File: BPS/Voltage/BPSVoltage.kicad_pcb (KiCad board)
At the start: 2 copper layers, 75 x 65 mm, 124 parts, among them J1 Conn1, J2 Conn2, J3 Conn_01x06, J4 Conn_01x07, J5 Conn_01x03, J6 Conn_01x05, J7 Conn_01x05, Q1 BSS308PE, Q10 BSS308PE, Q11 BSS308PE, Q12 BSS308PE, Q13 BSS308PE, Q2 BSS308PE, Q3 BSS308PE, Q4 BSS308PE, Q5 NSV1C201MZ4, Q6 BSS308PE, Q7 BSS308PE, Q8 BSS308PE, Q9 BSS308PE, U1 LTC6811-1, U2 HX1188FNL

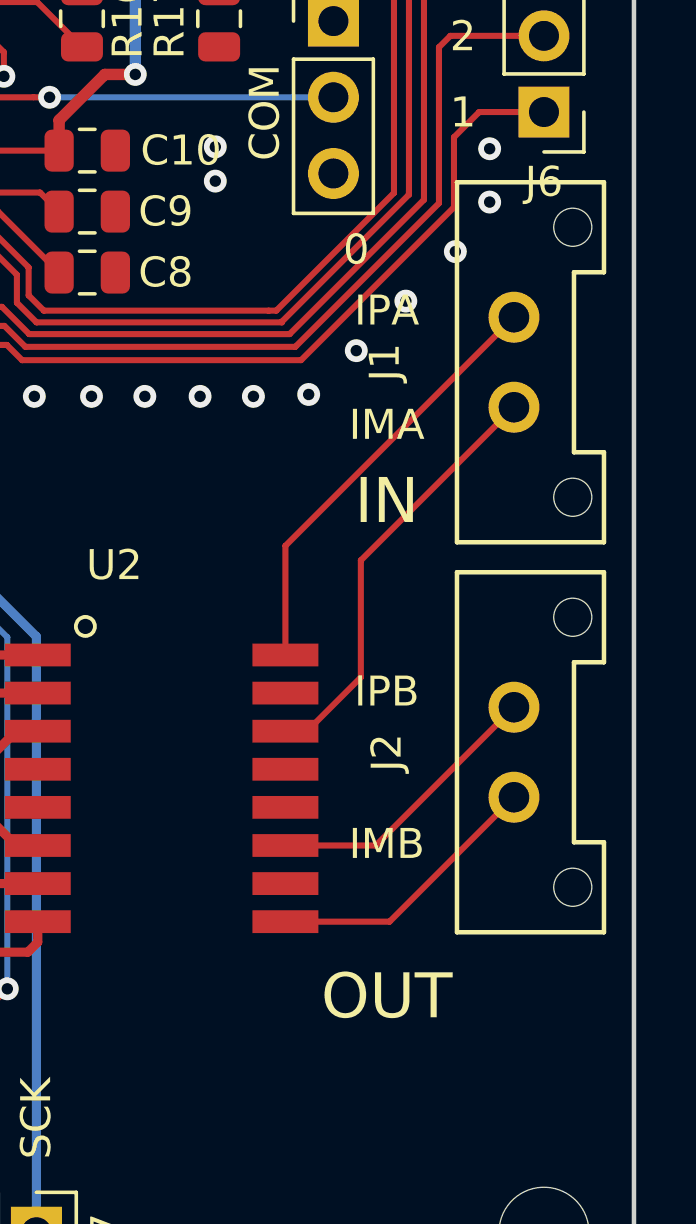
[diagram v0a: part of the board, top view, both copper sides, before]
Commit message: Changed the connectors to stack
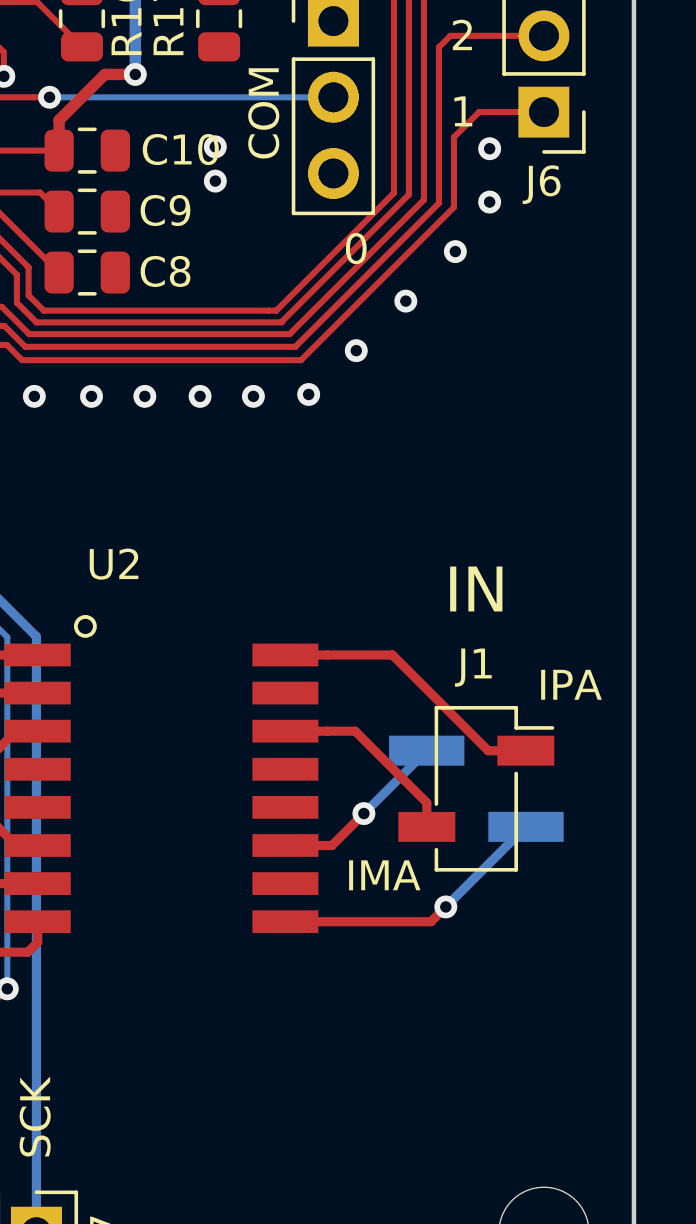
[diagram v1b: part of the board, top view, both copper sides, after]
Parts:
- J1: footprint UTSVT_Connectors:Molex_MicroFit3.0_1x2xP3.00mm_PolarizingPeg_Vertical -> Connector_PinSocket_2.54mm:PinSocket_1x02_P2.54mm_Vertical_SMD_Pin1Right
- J2: footprint UTSVT_Connectors:Molex_MicroFit3.0_1x2xP3.00mm_PolarizingPeg_Vertical -> Connector_PinHeader_2.54mm:PinHeader_1x02_P2.54mm_Vertical_SMD_Pin1Right; moved to B.Cu
- moved J1 15.8 mm to (114.7, 97.2), turned to 0 degrees
- moved J2 2.99 mm to (114.7, 97.2), turned to 180 degrees
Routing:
- net Net-(J1-Pad2): track 14.4 -> 6.51 mm
- net Net-(J1-Pad1): track 14.4 -> 9.33 mm
- net Net-(J2-Pad1): track 9.53 -> 6.02 mm, vias 0 -> 1
- net Net-(J2-Pad2): track 9.34 -> 9.33 mm, vias 0 -> 1

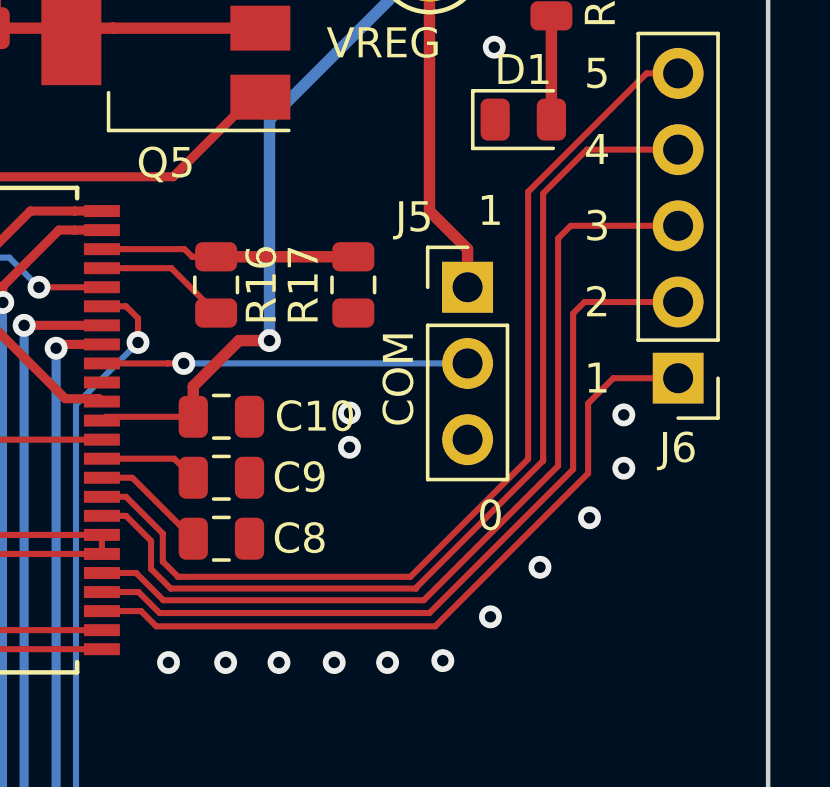
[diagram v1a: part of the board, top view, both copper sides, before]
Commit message: Edited comm pins of BPS voltage in case of stacking issues.
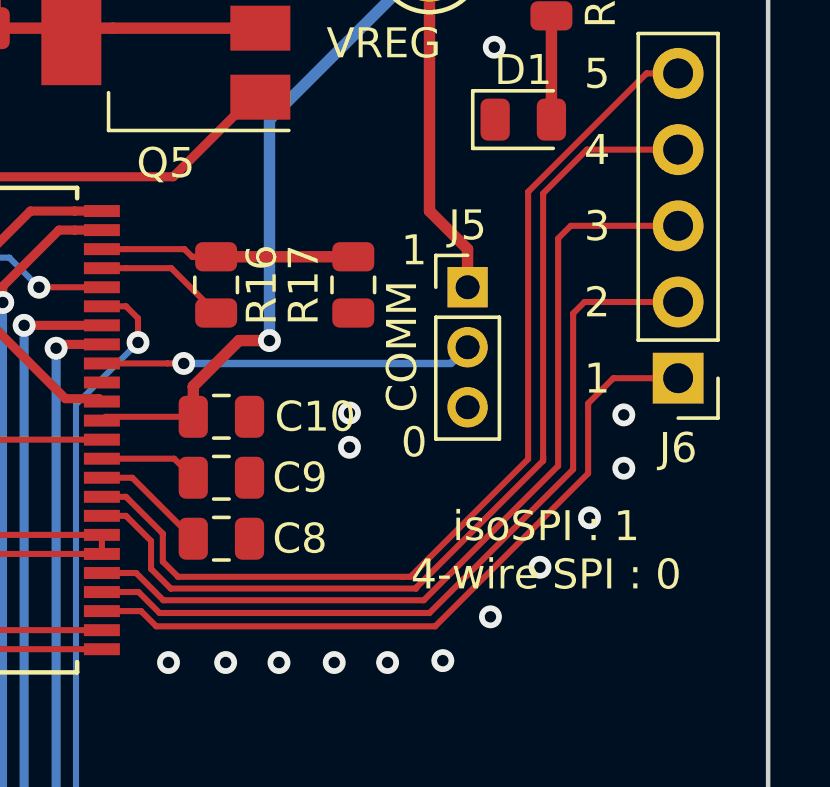
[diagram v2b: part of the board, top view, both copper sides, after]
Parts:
- J5: footprint Connector_PinHeader_2.54mm:PinHeader_1x03_P2.54mm_Vertical -> Connector_PinHeader_2.00mm:PinHeader_1x03_P2.00mm_Vertical
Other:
- board text added: "COMM"
- board text added: "isoSPI : 1 4-wire SPI : 0"
- board text removed: "COM"
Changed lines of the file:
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@@
   (general
     (thickness 1.6)
-    (drawings 38)
-    (tracks 661)
+    (drawings 39)
+    (tracks 662)
     (zones 0)
     (modules 124)
@@
   )
   (setup
-    (last_trace_width 0.3048)
+    (last_trace_width 0.25)
     (user_trace_width 0.2032)
     (user_trace_width 0.254)
@@
     (add_net "Net-(R16-Pad2)")
   )
+  (module Connector_PinHeader_2.00mm:PinHeader_1x03_P2.00mm_Vertical (layer F.Cu)
+    (at 109.982 71.628)
+    (descr "Through hole straight pin header, 1x03, 2.00mm pitch, single row")
+    (tags "Through hole pin header THT 1x03 2.00mm single row")
+    (fp_text reference J5 (at 0 -2.06) (layer F.SilkS)
+      (effects (font (size 1 1) (thickness 0.15)))
+    )
+    (fp_text value Conn_01x03 (at 0 6.06) (layer F.Fab)
+      (effects (font (size 1 1) (thickness 0.15)))
+    )
+    (fp_text user %R (at 0 2 90) (layer F.Fab)
+      (effects (font (size 1 1) (thickness 0.15)))
+    )
+    (fp_line (start 1.5 -1.5) (end -1.5 -1.5) (layer F.CrtYd) (width 0.05))
+    (fp_line (start 1.5 5.5) (end 1.5 -1.5) (layer F.CrtYd) (width 0.05))
+    (fp_line (start -1.5 5.5) (end 1.5 5.5) (layer F.CrtYd) (width 0.05))
+    (fp_line (start -1.5 -1.5) (end -1.5 5.5) (layer F.CrtYd) (width 0.05))
+    (fp_line (start -1.06 -1.06) (end 0 -1.06) (layer F.SilkS) (width 0.12))
+    (fp_line (start -1.06 0) (end -1.06 -1.06) (layer F.SilkS) (width 0.12))
+    (fp_line (start -1.06 1) (end 1.06 1) (layer F.SilkS) (width 0.12))
+    (fp_line (start 1.06 1) (end 1.06 5.06) (layer F.SilkS) (width 0.12))
+    (fp_line (start -1.06 1) (end -1.06 5.06) (layer F.SilkS) (width 0.12))
+    (fp_line (start -1.06 5.06) (end 1.06 5.06) (layer F.SilkS) (width 0.12))
+    (fp_line (start -1 -0.5) (end -0.5 -1) (layer F.Fab) (width 0.1))
+    (fp_line (start -1 5) (end -1 -0.5) (layer F.Fab) (width 0.1))
+    (fp_line (start 1 5) (end -1 5) (layer F.Fab) (width 0.1))
+    (fp_line (start 1 -1) (end 1 5) (layer F.Fab) (width 0.1))
+    (fp_line (start -0.5 -1) (end 1 -1) (layer F.Fab) (width 0.1))
+    (pad 3 thru_hole oval (at 0 4) (size 1.35 1.35) (drill 0.8) (layers *.Cu *.Mask)
+      (net 2 GND))
+    (pad 2 thru_hole oval (at 0 2) (size 1.35 1.35) (drill 0.8) (layers *.Cu *.Mask)
+      (net 59 /ISOMD))
+    (pad 1 thru_hole rect (at 0 0) (size 1.35 1.35) (drill 0.8) (layers *.Cu *.Mask)
+      (net 12 /VREG))
+    (model ${KISYS3DMOD}/Connector_PinHeader_2.00mm.3dshapes/PinHeader_1x03_P2.00mm_Vertical.wrl
+      (at (xyz 0 0 0))
+      (scale (xyz 1 1 1))
+      (rotate (xyz 0 0 0))
+    )
+  )
   (module MountingHole:MountingHole_3mm (layer F.Cu)
     (at 48 53)
@@
     )
   )
-  (module Connector_PinHeader_2.54mm:PinHeader_1x03_P2.54mm_Vertical (layer F.Cu)
-    (at 109.982 71.628)
-    (descr "Through hole straight pin header, 1x03, 2.54mm pitch, single row")
-    (tags "Through hole pin header THT 1x03 2.54mm single row")
-    (fp_text reference J5 (at -1.778 -2.33) (layer F.SilkS)
-      (effects (font (size 1 1) (thickness 0.15)))
-    )
-    (fp_text value Conn_01x03 (at 0 7.41) (layer F.Fab)
-      (effects (font (size 1 1) (thickness 0.15)))
-    )
-    (fp_line (start -0.635 -1.27) (end 1.27 -1.27) (layer F.Fab) (width 0.1))
-    (fp_line (start 1.27 -1.27) (end 1.27 6.35) (layer F.Fab) (width 0.1))
-    (fp_line (start 1.27 6.35) (end -1.27 6.35) (layer F.Fab) (width 0.1))
-    (fp_line (start -1.27 6.35) (end -1.27 -0.635) (layer F.Fab) (width 0.1))
-    (fp_line (start -1.27 -0.635) (end -0.635 -1.27) (layer F.Fab) (width 0.1))
-    (fp_line (start -1.33 6.41) (end 1.33 6.41) (layer F.SilkS) (width 0.12))
-    (fp_line (start -1.33 1.27) (end -1.33 6.41) (layer F.SilkS) (width 0.12))
-    (fp_line (start 1.33 1.27) (end 1.33 6.41) (layer F.SilkS) (width 0.12))
-    (fp_line (start -1.33 1.27) (end 1.33 1.27) (layer F.SilkS) (width 0.12))
-    (fp_line (start -1.33 0) (end -1.33 -1.33) (layer F.SilkS) (width 0.12))
-    (fp_line (start -1.33 -1.33) (end 0 -1.33) (layer F.SilkS) (width 0.12))
-    (fp_line (start -1.8 -1.8) (end -1.8 6.85) (layer F.CrtYd) (width 0.05))
-    (fp_line (start -1.8 6.85) (end 1.8 6.85) (layer F.CrtYd) (width 0.05))
-    (fp_line (start 1.8 6.85) (end 1.8 -1.8) (layer F.CrtYd) (width 0.05))
-    (fp_line (start 1.8 -1.8) (end -1.8 -1.8) (layer F.CrtYd) (width 0.05))
-    (fp_text user %R (at 0 2.54 90) (layer F.Fab)
-      (effects (font (size 1 1) (thickness 0.15)))
-    )
-    (pad 1 thru_hole rect (at 0 0) (size 1.7 1.7) (drill 1) (layers *.Cu *.Mask)
-      (net 12 /VREG))
-    (pad 2 thru_hole oval (at 0 2.54) (size 1.7 1.7) (drill 1) (layers *.Cu *.Mask)
-      (net 59 /ISOMD))
-    (pad 3 thru_hole oval (at 0 5.08) (size 1.7 1.7) (drill 1) (layers *.Cu *.Mask)
-      (net 2 GND))
-    (model ${KISYS3DMOD}/Connector_PinHeader_2.54mm.3dshapes/PinHeader_1x03_P2.54mm_Vertical.wrl
-      (at (xyz 0 0 0))
-      (scale (xyz 1 1 1))
-      (rotate (xyz 0 0 0))
-    )
-  )
   (module Connector_PinHeader_2.54mm:PinHeader_1x05_P2.54mm_Vertical (layer F.Cu)
     (at 117 74.66 180)
@@
     )
   )
+  (gr_text "isoSPI : 1\n4-wire SPI : 0" (at 112.6 80.4) (layer F.SilkS)
+    (effects (font (size 1 1) (thickness 0.15)))
+  )
   (gr_text "Dr. Gary Hallock" (at 99.1 102.35) (layer B.SilkS)
     (effects (font (size 1.5 1.5) (thickness 0.3)) (justify mirror))
@@
     (effects (font (size 1 1) (thickness 0.15)))
   )
-  (gr_text COM (at 107.696 74.676 90) (layer F.SilkS)
+  (gr_text COMM (at 107.8 73.6 90) (layer F.SilkS)
     (effects (font (size 1 1) (thickness 0.15)))
   )
-  (gr_text 1 (at 110.744 69.088) (layer F.SilkS)
+  (gr_text 1 (at 108.2 70.4) (layer F.SilkS)
     (effects (font (size 1 1) (thickness 0.15)))
   )
-  (gr_text 0 (at 110.744 79.248) (layer F.SilkS)
+  (gr_text 0 (at 108.2 76.8) (layer F.SilkS)
     (effects (font (size 1 1) (thickness 0.15)))
   )
@@
   (segment (start 103.378 73.406) (end 103.378 66.04) (width 0.381) (layer B.Cu) (net 12))
   (segment (start 108.712 60.706) (end 108.712 69.088) (width 0.381) (layer F.Cu) (net 12) (status 10))
-  (segment (start 109.982 70.358) (end 109.982 71.628) (width 0.381) (layer F.Cu) (net 12) (status 20))
   (segment (start 108.712 69.088) (end 109.982 70.358) (width 0.381) (layer F.Cu) (net 12))
+  (segment (start 109.982 70.358) (end 109.982 71.782) (width 0.381) (layer F.Cu) (net 12))
   (via (at 74.676 81.05546) (size 0.762) (drill 0.381) (layers F.Cu B.Cu) (net 13))
   (segment (start 74.58557 80.96503) (end 74.676 81.05546) (width 0.381) (layer F.Cu) (net 13))
@@
   (segment (start 112.776 62.581) (end 112.776 66.04) (width 0.381) (layer F.Cu) (net 58) (status 30))
   (via (at 100.5205 74.168) (size 0.762) (drill 0.381) (layers F.Cu B.Cu) (net 59))
-  (segment (start 109.982 74.168) (end 100.5205 74.168) (width 0.2032) (layer B.Cu) (net 59) (status 10))
   (segment (start 99.981685 74.168) (end 97.792 74.168) (width 0.2032) (layer F.Cu) (net 59) (status 20))
   (segment (start 100.5205 74.168) (end 99.981685 74.168) (width 0.2032) (layer F.Cu) (net 59))
+  (segment (start 100.5205 74.168) (end 109.432 74.168) (width 0.25) (layer B.Cu) (net 59))
+  (segment (start 109.432 74.168) (end 110 73.6) (width 0.25) (layer B.Cu) (net 59))
   (segment (start 99.822 79.8398) (end 98.5952 78.613) (width 0.2032) (layer F.Cu) (net 60))
   (segment (start 99.822 80.772) (end 99.822 79.8398) (width 0.2032) (layer F.Cu) (net 60))

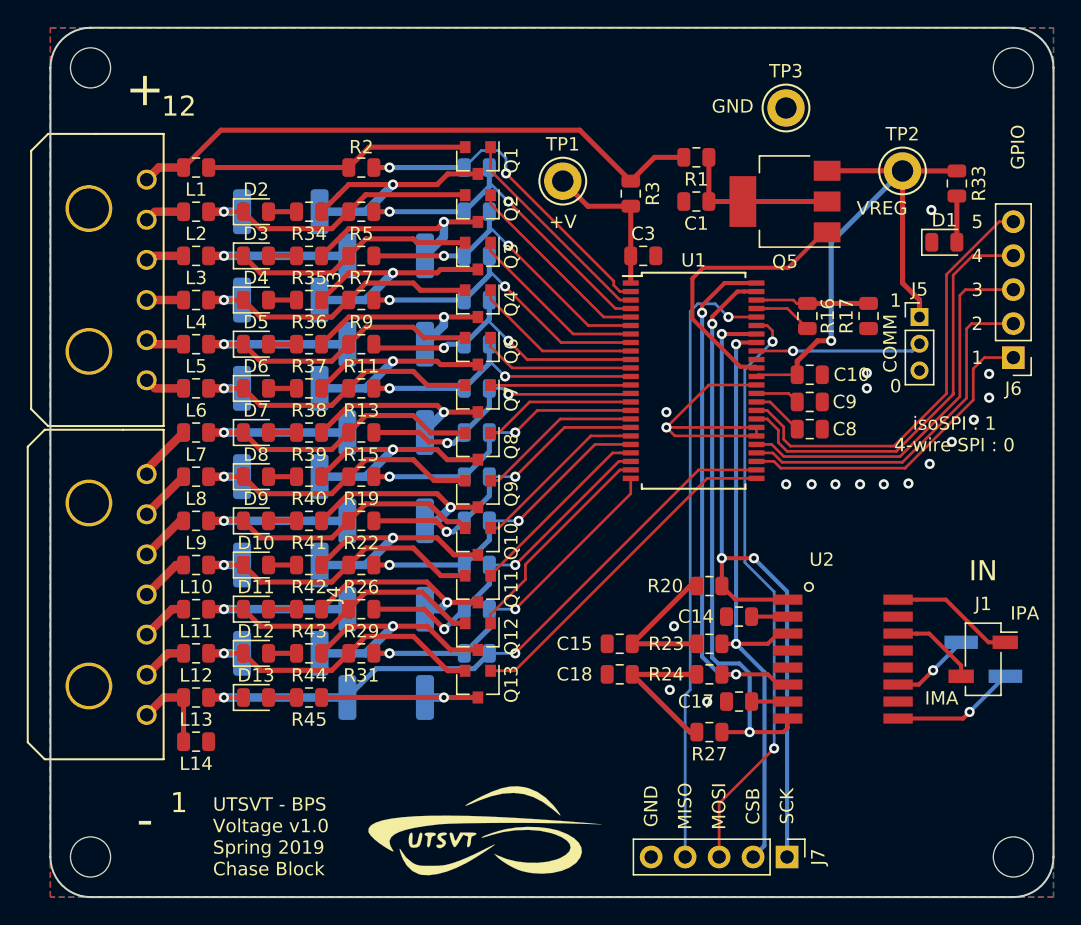
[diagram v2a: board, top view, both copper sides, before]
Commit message: Redid the footprint for the IC, rerouted.
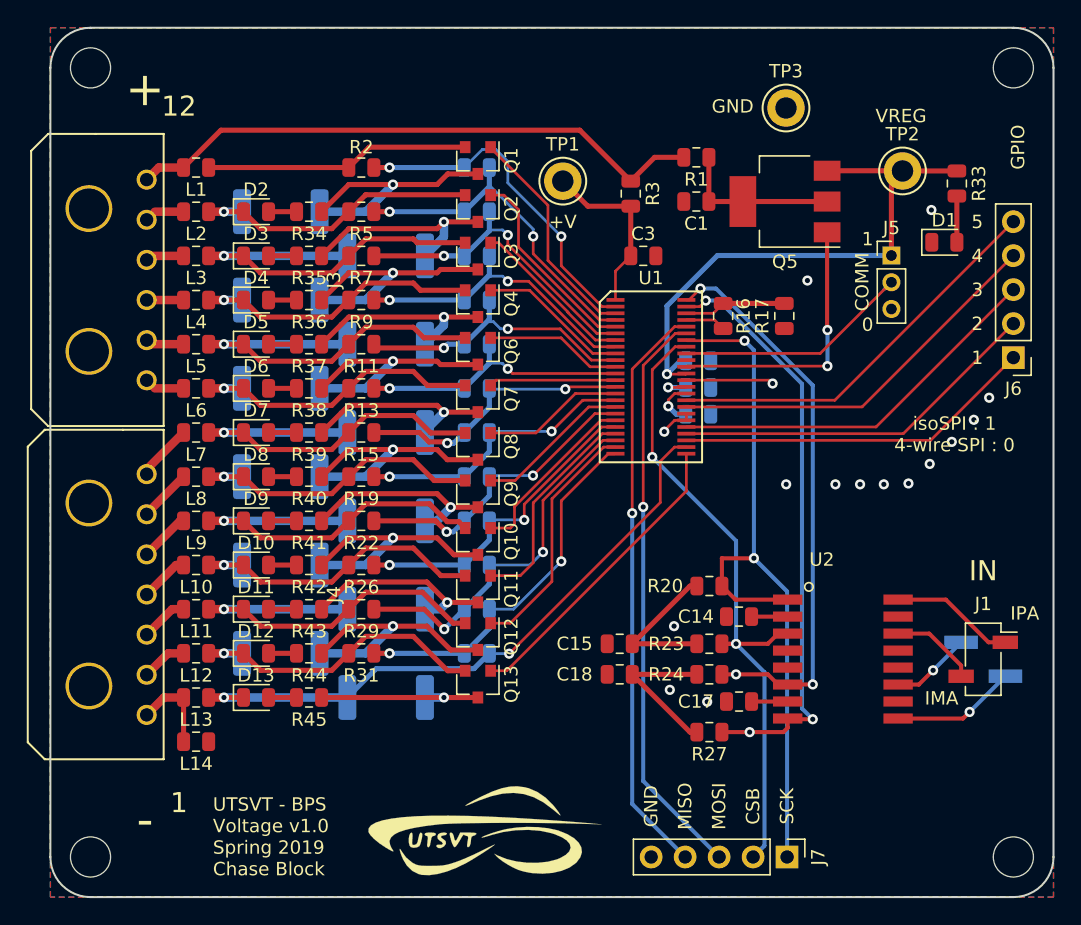
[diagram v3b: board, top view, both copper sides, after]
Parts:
- C10, C8, C9: moved to B.Cu
- U1: footprint Package_SO:SSOP-48_7.5x15.9mm_P0.635mm -> UTSVT_ICs:SOIC-48
- moved C8 8.41 mm to (93.4, 78.9)
- moved C9 8.41 mm to (93.4, 76.9)
- moved C10 8.40 mm to (93.4, 74.9)
- moved G*** 7.25 mm to (102.0, 91.5)
- moved R16 6.30 mm to (95.3, 71.5)
- moved R17 6.30 mm to (99.9, 71.5)
- moved J5 5.06 mm to (107.9, 67.0)
- moved U1 3.21 mm to (89.9, 76.1), turned to 270 degrees
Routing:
- net GND: track 22.4 -> 9.10 mm, vias 19 -> 16
- net /ISOMD: track 12.4 -> 18.3 mm, vias 1 -> 0
- net /SDO: track 46.5 -> 43.5 mm
- net /GPIO4: track 32.2 -> 29.1 mm
- net /GPIO5: track 33.0 -> 30.0 mm
- net /IPB: track 39.3 -> 42.3 mm, vias 2 -> 3
- net Net-(Q13-Pad1): track 25.8 -> 23.0 mm
- net /GPIO1: track 24.2 -> 27.0 mm
- net /Batt0: track 49.5 -> 46.8 mm
- net Net-(C11-Pad2): track 23.1 -> 20.6 mm
- net /IMA: track 46.4 -> 48.8 mm
- net Net-(Q12-Pad1): track 16.3 -> 18.4 mm
- net Net-(Q11-Pad1): track 14.3 -> 16.4 mm
- net Net-(C19-Pad1): track 25.9 -> 27.6 mm
- net Net-(C3-Pad1): track 11.6 -> 13.3 mm
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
